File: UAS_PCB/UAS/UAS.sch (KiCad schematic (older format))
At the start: 0 parts

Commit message: uas pcb files updated to latest version in ranis hellscape
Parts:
- added J1, J2, J3, J4: SM02B-PASS-TBT, UAS:JST_SM02B-PASS-TBT(LF)(SN), symbol UAS-rescue:SM02B-PASS-TBT-UAS-cache
- added U1, U8: JST-7-Pin, UAS:JST_SM07B-PASS-TBT(LF)(SN), symbol UAS-rescue:JST-7-Pin-UAS-cache
- added U10: UAS-rescue_7.5V-2.4A-Converter-UAS-cache, UAS:Pololu_7.75V_2.4A_Step_Down_Regulator, symbol UAS-rescue:UAS-rescue_7.5V-2.4A-Converter-UAS-cache-UAS-cache
- added U11, U9: JST-3-Pin, UAS:JST_SM03B-PASS-TBT(LF)(SN), symbol UAS-rescue:JST-3-Pin-UAS-cache
- added U12, U13: Signal-Pad, UAS:Individual_Solder_Pad, symbol UAS-rescue:Signal-Pad-UAS-cache
- added U14, U15, U16, U17: UAS-rescue_Signal-Pad-UAS-cache, UAS:Individual_Solder_Pad, symbol UAS-cache:UAS-rescue_Signal-Pad-UAS-cache
- added U2: 5A-5V-Converter, UAS:Pololu_5V_5A_Step_Down_Regulator, symbol UAS-rescue:5A-5V-Converter-UAS-cache
- added U3: 500mA-5V-Converter, UAS:Pololu_5V_500mA_Step_Down_Regulator, symbol UAS-rescue:500mA-5V-Converter-UAS-cache
- added U4: 12V-StepUp-Converter, UAS:Pololu_12V_Step_Up_Voltage_Regulator_SMT, symbol UAS-rescue:12V-StepUp-Converter-UAS-cache
- added U5: TB6612FNG-Dual-Motor-Driver, UAS:Pololu_TB6612_Dual_Motor_Driver_Carrier_SMT, symbol UAS-rescue:TB6612FNG-Dual-Motor-Driver-UAS-cache
- added U6: 16_Pad_2x8_Set-UAS-cache, UAS:16_Pad_Set_2mm_pitch, symbol UAS-rescue:UAS-rescue_16_Pad_2x8_Set-UAS-cache-UAS-cache
- added U7: UAS-rescue_JST-4-Pin-UAS-cache, UAS:JST_XH_B4B-XH-A_1x04_P2.50mm_Vertical, symbol UAS-rescue:UAS-rescue_JST-4-Pin-UAS-cache-UAS-cache
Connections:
- net labels added: +12V, +5V, +7.5V, GND
- wire segments 0 -> 141

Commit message: UAS Schematic/Footprint Updates
Nothing for the board layout has been worked on yet, schematic is done except for stuff like diodes or whatever I haven't confirmed w/ u guys
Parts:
- removed J1, J2, J3, J4: SM02B-PASS-TBT, UAS:JST_SM02B-PASS-TBT(LF)(SN), symbol UAS-rescue:SM02B-PASS-TBT-UAS-cache
- removed U1, U8: JST-7-Pin, UAS:JST_SM07B-PASS-TBT(LF)(SN), symbol UAS-rescue:JST-7-Pin-UAS-cache
- removed U6: 16_Pad_2x8_Set-UAS-cache, UAS:16_Pad_Set_2mm_pitch, symbol UAS-rescue:UAS-rescue_16_Pad_2x8_Set-UAS-cache-UAS-cache
- added J1, J3, J6, J7: SM04B-GHS-TB(LF)(SN)-, JST_SM04B-GHS-TB(LF)(SN)-, symbol UAS:SM04B-GHS-TB(LF)(SN)-
- added J2, J8: SM07B-GHS-TB(LF)(SN), JST_SM07B-GHS-TB(LF)(SN), symbol UAS:SM07B-GHS-TB(LF)(SN)
- added J4: SM08B-GHS-TB(LF)(SN), UAS:JST_SM08B-GHS-TB(LF)(SN), symbol UAS:SM08B-GHS-TB(LF)(SN)
- added J5: SM08B-GHS-TB(LF)(SN), JST_SM08B-GHS-TB(LF)(SN), symbol UAS:SM08B-GHS-TB(LF)(SN)
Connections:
- wire segments 141 -> 179

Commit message: Updates To UAS PCB
update #based
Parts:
- added D1, D2: D, Diode_SMD:D_0603_1608Metric, symbol Device:D
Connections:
- net at U13.1 (Signal_Out), U9.3: now also D1.1 (K), D1.2 (A)
- net at U11.3, U12.1 (Signal_Out): now also D2.1 (K), D2.2 (A)
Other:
- moved on the sheet: U12, U13
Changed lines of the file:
@@
 	5550 4900 6250 4900
-Wire Wire Line
-	6250 4900 6250 6400
 Wire Wire Line
 	6250 6400 3350 6400
@@
 L UAS-rescue:Signal-Pad-UAS-cache U12
 U 1 1 60391DEE
-P 4250 5500
-F 0 "U12" H 4328 5759 50  0000 L CNN
-F 1 "Signal-Pad" H 4328 5668 50  0000 L CNN
-F 2 "UAS:Individual_Solder_Pad" H 4250 5500 50  0001 C CNN
-F 3 "" H 4250 5500 50  0001 C CNN
-	1    4250 5500
+P 4250 5300
+F 0 "U12" H 4328 5559 50  0000 L CNN
+F 1 "Signal-Pad" H 4328 5468 50  0000 L CNN
+F 2 "UAS:Individual_Solder_Pad" H 4250 5300 50  0001 C CNN
+F 3 "" H 4250 5300 50  0001 C CNN
+	1    4250 5300
 	1    0    0    -1
 $EndComp
@@
 L UAS-rescue:Signal-Pad-UAS-cache U13
 U 1 1 60392D35
-P 4450 5500
-F 0 "U13" H 4528 5759 50  0000 L CNN
-F 1 "Signal-Pad" H 4528 5668 50  0000 L CNN
-F 2 "UAS:Individual_Solder_Pad" H 4450 5500 50  0001 C CNN
-F 3 "" H 4450 5500 50  0001 C CNN
-	1    4450 5500
-	1    0    0    -1
-$EndComp
-Wire Wire Line
-	4250 5600 4250 5900
-Wire Wire Line
-	4250 5900 5600 5900
+P 4450 5300
+F 0 "U13" H 4528 5559 50  0000 L CNN
+F 1 "Signal-Pad" H 4528 5468 50  0000 L CNN
+F 2 "UAS:Individual_Solder_Pad" H 4450 5300 50  0001 C CNN
+F 3 "" H 4450 5300 50  0001 C CNN
+	1    4450 5300
+	1    0    0    -1
+$EndComp
 Wire Wire Line
 	5600 5900 5600 5550
-Wire Wire Line
-	4850 5550 4850 5700
-Wire Wire Line
-	4850 5700 4450 5700
-Wire Wire Line
-	4450 5700 4450 5600
 $Comp
 L power:GND #PWR0101
@@
 $EndComp
 Connection ~ 5350 6000
-$Comp
-L UAS-cache:UAS-rescue_Signal-Pad-UAS-cache U17
-U 1 1 603DAF7F
-P 5600 3750
-F 0 "U17" H 5512 3916 50  0000 R CNN
-F 1 "UAS-rescue_Signal-Pad-UAS-cache" H 5512 4007 50  0000 R CNN
-F 2 "UAS:Individual_Solder_Pad" H 5600 3750 50  0001 C CNN
-F 3 "" H 5600 3750 50  0001 C CNN
-	1    5600 3750
-	-1   0    0    1
-$EndComp
-$Comp
-L UAS-cache:UAS-rescue_Signal-Pad-UAS-cache U15
-U 1 1 603D9E61
-P 5300 3750
-F 0 "U15" H 5212 3916 50  0000 R CNN
-F 1 "UAS-rescue_Signal-Pad-UAS-cache" H 5212 4007 50  0000 R CNN
-F 2 "UAS:Individual_Solder_Pad" H 5300 3750 50  0001 C CNN
-F 3 "" H 5300 3750 50  0001 C CNN
-	1    5300 3750
-	-1   0    0    1
-$EndComp
-$Comp
-L UAS-cache:UAS-rescue_Signal-Pad-UAS-cache U16
-U 1 1 603D9324
-P 5600 3350
-F 0 "U16" H 5678 3609 50  0000 L CNN
-F 1 "UAS-rescue_Signal-Pad-UAS-cache" H 5678 3518 50  0000 L CNN
-F 2 "UAS:Individual_Solder_Pad" H 5600 3350 50  0001 C CNN
-F 3 "" H 5600 3350 50  0001 C CNN
-	1    5600 3350
-	1    0    0    -1
-$EndComp
-$Comp
-L UAS-cache:UAS-rescue_Signal-Pad-UAS-cache U14
-U 1 1 603D8772
-P 5300 3350
-F 0 "U14" H 5378 3609 50  0000 L CNN
-F 1 "UAS-rescue_Signal-Pad-UAS-cache" H 5378 3518 50  0000 L CNN
-F 2 "UAS:Individual_Solder_Pad" H 5300 3350 50  0001 C CNN
-F 3 "" H 5300 3350 50  0001 C CNN
-	1    5300 3350
-	1    0    0    -1
-$EndComp
-Wire Wire Line
-	5300 3450 5300 3650
-Wire Wire Line
-	5600 3450 5600 3650
 $Comp
 L UAS:SM07B-GHS-TB(LF)(SN) J2
@@
 	0    -1   -1   0
 $EndComp
+Wire Wire Line
+	6250 4900 6250 6400
+$Comp
+L Device:D D2
+U 1 1 606E7312
+P 4650 6050
+F 0 "D2" H 4650 5834 50  0000 C CNN
+F 1 "D" H 4650 5925 50  0000 C CNN
+F 2 "Diode_SMD:D_0603_1608Metric" H 4650 6050 50  0001 C CNN
+F 3 "~" H 4650 6050 50  0001 C CNN
+	1    4650 6050
+	-1   0    0    1
+$EndComp
+Wire Wire Line
+	4850 5550 4850 5600
+$Comp
+L Device:D D1
+U 1 1 6073A3FE
+P 4650 5700
+F 0 "D1" H 4650 5484 50  0000 C CNN
+F 1 "D" H 4650 5575 50  0000 C CNN
+F 2 "Diode_SMD:D_0603_1608Metric" H 4650 5700 50  0001 C CNN
+F 3 "~" H 4650 5700 50  0001 C CNN
+	1    4650 5700
+	-1   0    0    1
+$EndComp
+Wire Wire Line
+	4450 5600 4450 5400
+Wire Wire Line
+	4250 5400 4250 5900
+Wire Wire Line
+	5600 3450 5600 3650
+Wire Wire Line
+	5300 3450 5300 3650
+$Comp
+L UAS-cache:UAS-rescue_Signal-Pad-UAS-cache U14
+U 1 1 603D8772
+P 5300 3350
+F 0 "U14" H 5378 3609 50  0000 L CNN
+F 1 "UAS-rescue_Signal-Pad-UAS-cache" H 5378 3518 50  0000 L CNN
+F 2 "UAS:Individual_Solder_Pad" H 5300 3350 50  0001 C CNN
+F 3 "" H 5300 3350 50  0001 C CNN
+	1    5300 3350
+	1    0    0    -1
+$EndComp
+$Comp
+L UAS-cache:UAS-rescue_Signal-Pad-UAS-cache U16
+U 1 1 603D9324
+P 5600 3350
+F 0 "U16" H 5678 3609 50  0000 L CNN
+F 1 "UAS-rescue_Signal-Pad-UAS-cache" H 5678 3518 50  0000 L CNN
+F 2 "UAS:Individual_Solder_Pad" H 5600 3350 50  0001 C CNN
+F 3 "" H 5600 3350 50  0001 C CNN
+	1    5600 3350
+	1    0    0    -1
+$EndComp
+$Comp
+L UAS-cache:UAS-rescue_Signal-Pad-UAS-cache U15
+U 1 1 603D9E61
+P 5300 3750
+F 0 "U15" H 5212 3916 50  0000 R CNN
+F 1 "UAS-rescue_Signal-Pad-UAS-cache" H 5212 4007 50  0000 R CNN
+F 2 "UAS:Individual_Solder_Pad" H 5300 3750 50  0001 C CNN
+F 3 "" H 5300 3750 50  0001 C CNN
+	1    5300 3750
+	-1   0    0    1
+$EndComp
+$Comp
+L UAS-cache:UAS-rescue_Signal-Pad-UAS-cache U17
+U 1 1 603DAF7F
+P 5600 3750
+F 0 "U17" H 5512 3916 50  0000 R CNN
+F 1 "UAS-rescue_Signal-Pad-UAS-cache" H 5512 4007 50  0000 R CNN
+F 2 "UAS:Individual_Solder_Pad" H 5600 3750 50  0001 C CNN
+F 3 "" H 5600 3750 50  0001 C CNN
+	1    5600 3750
+	-1   0    0    1
+$EndComp
+Wire Wire Line
+	4250 5900 4450 5900
+Wire Wire Line
+	4800 6050 4850 6050
+Wire Wire Line
+	4850 6050 4850 5900
+Connection ~ 4850 5900
+Wire Wire Line
+	4850 5900 5600 5900
+Wire Wire Line
+	4500 6050 4450 6050
+Wire Wire Line
+	4450 6050 4450 5900
+Connection ~ 4450 5900
+Wire Wire Line
+	4450 5900 4850 5900
+Wire Wire Line
+	4500 5700 4450 5700
+Wire Wire Line
+	4450 5700 4450 5600
+Connection ~ 4450 5600
+Wire Wire Line
+	4450 5600 4850 5600
+Wire Wire Line
+	4800 5700 4850 5700
+Wire Wire Line
+	4850 5700 4850 5600
+Connection ~ 4850 5600
 $EndSCHEMATC

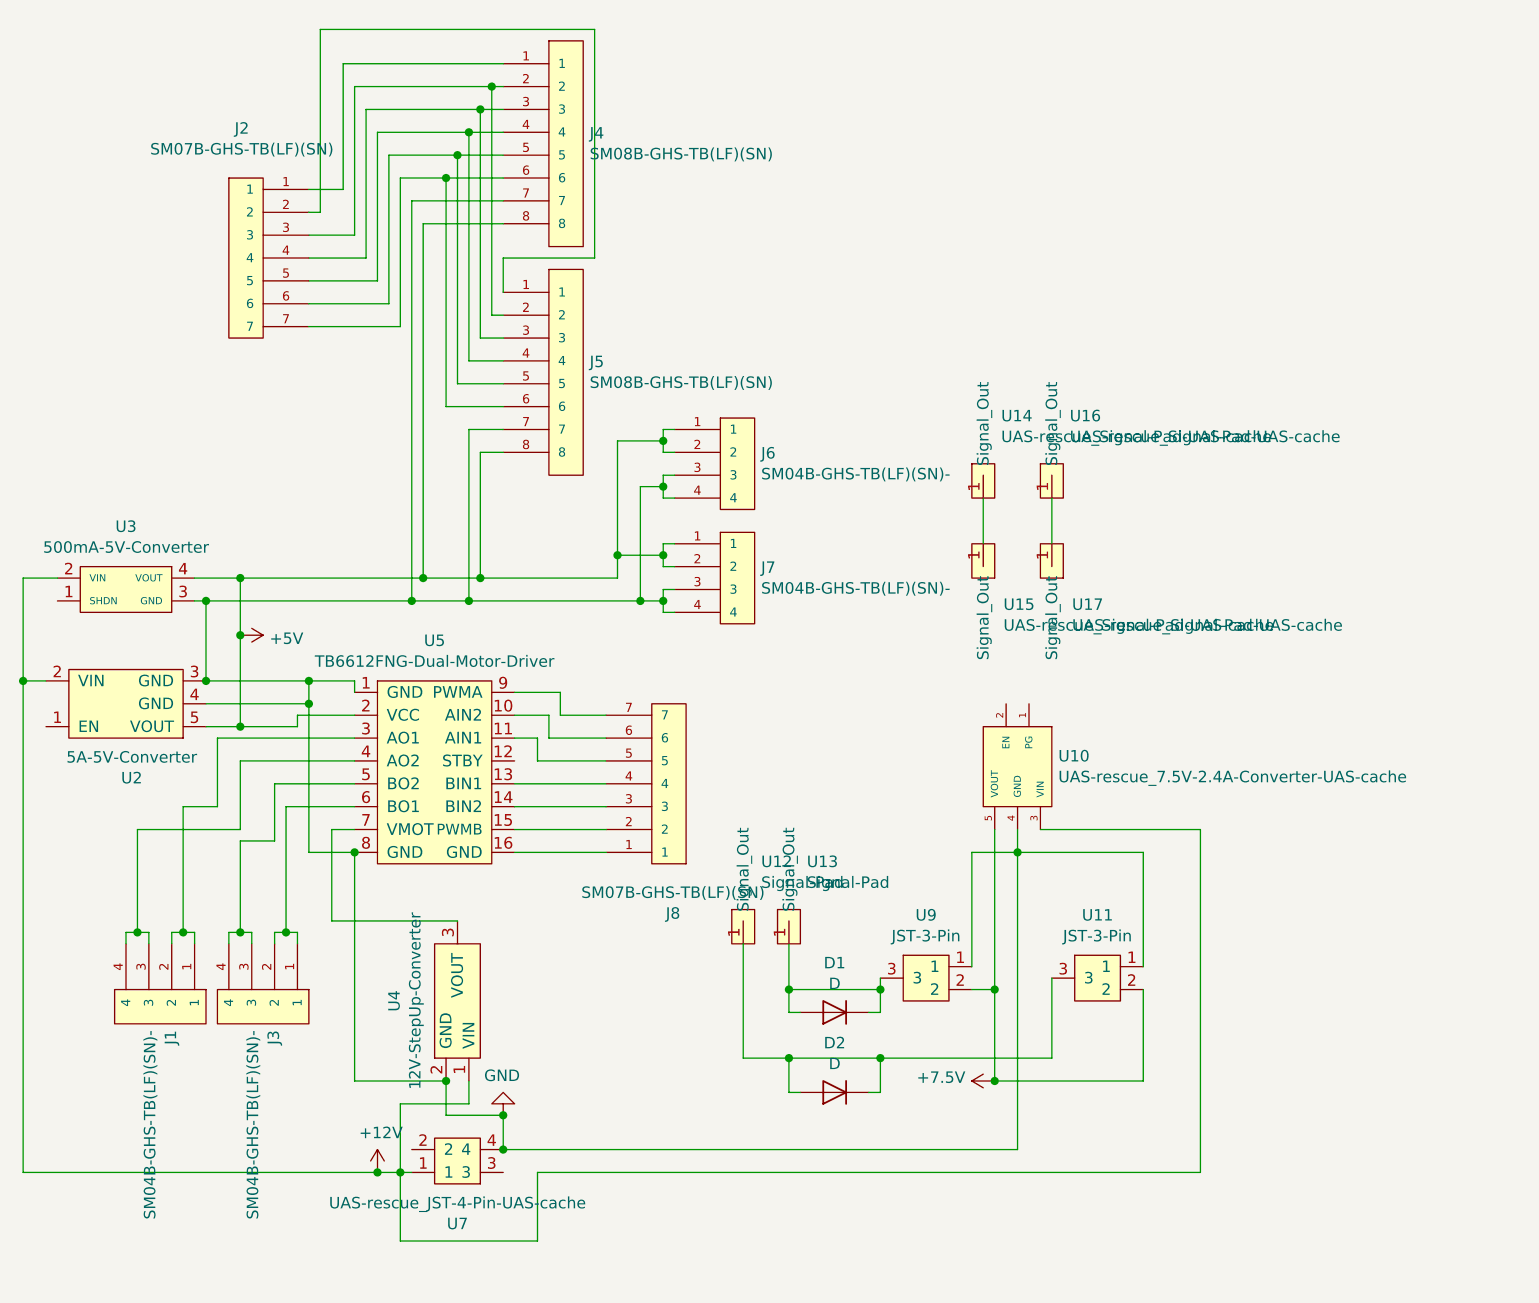
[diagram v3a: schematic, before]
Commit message: Removing Diodes
Just removing the diodes from schematic
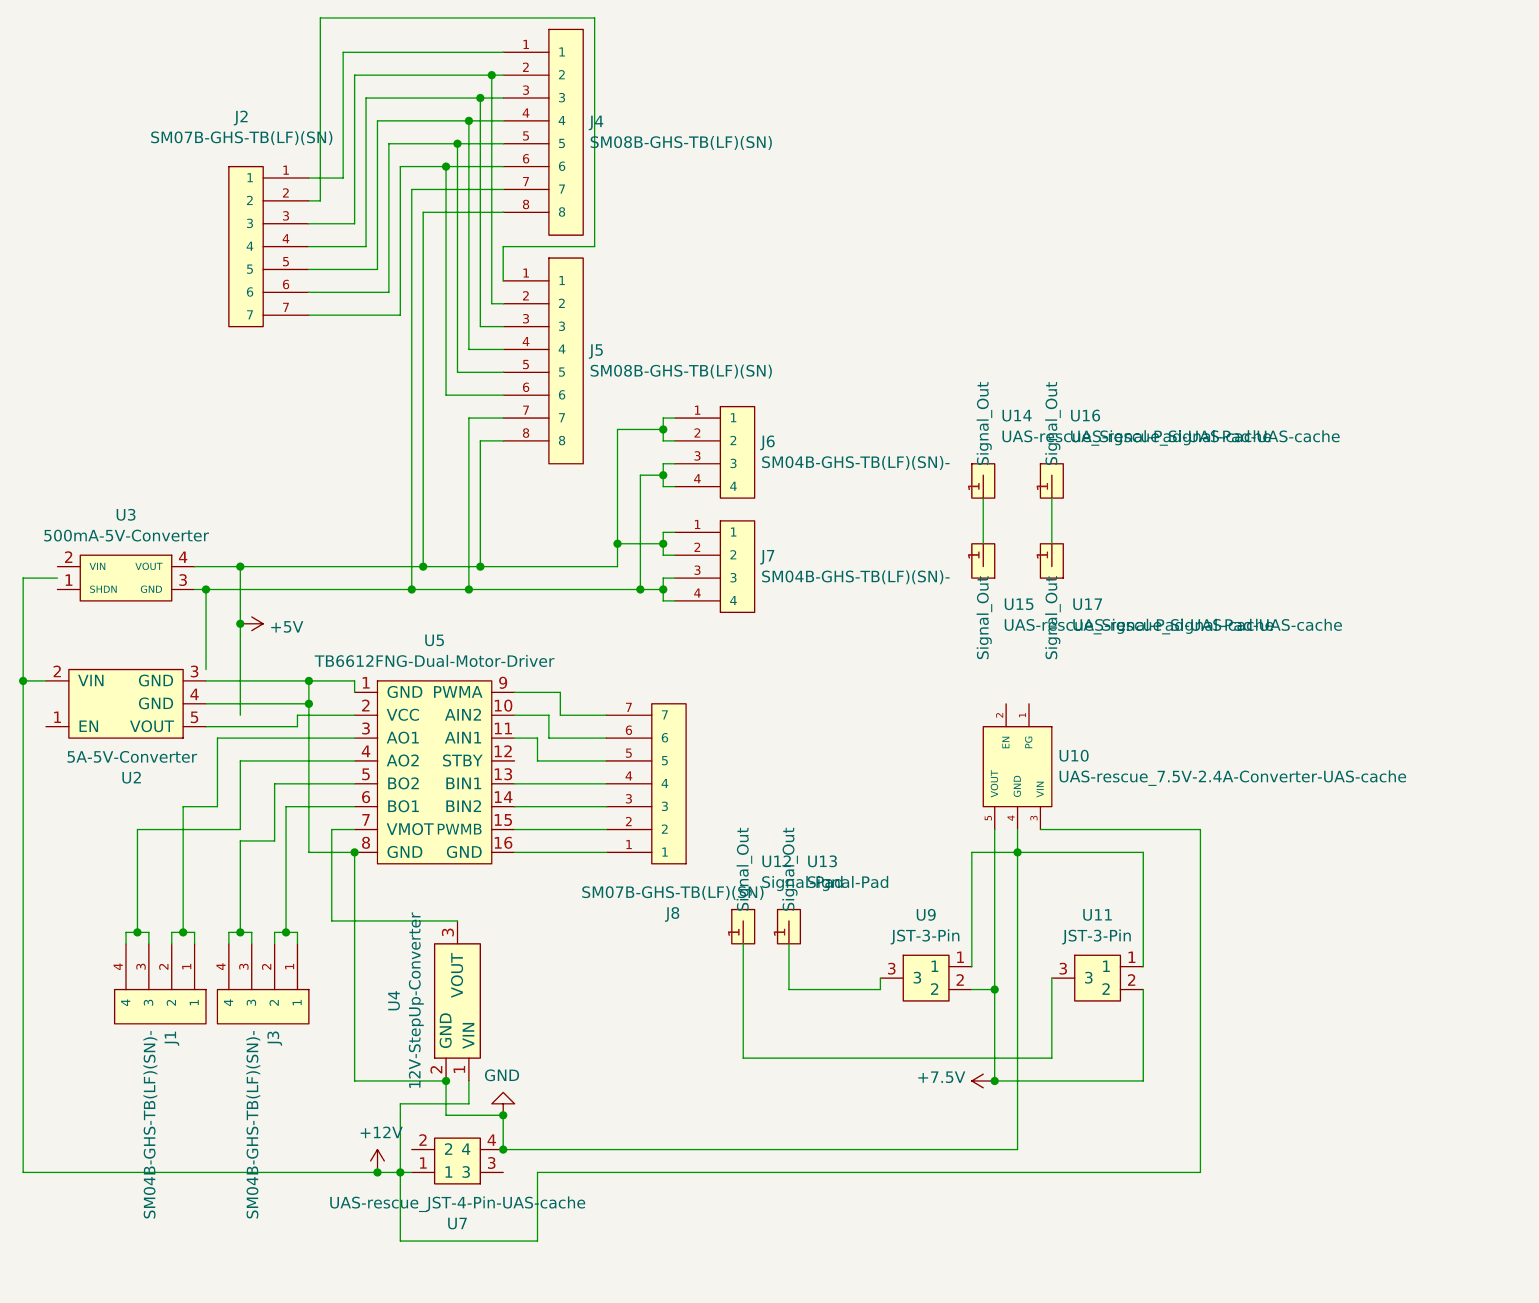
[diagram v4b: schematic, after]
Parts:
- removed D1, D2: D, Diode_SMD:D_0603_1608Metric, symbol Device:D
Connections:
- net +12V: no longer U3.2 (VIN)
- net +5V: no longer U2.5 (VOUT), U5.2 (VCC)
- net GND: no longer J4.7, J5.7, J6.3, J6.4, J7.3, J7.4, U3.3 (GND)
- new net: U2.5 (VOUT), U5.2 (VCC)
- new net: J4.7, J5.7, J6.3, J6.4, J7.3, J7.4, U3.3 (GND)
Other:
- moved on the sheet: J2, J4, J5, J6, J7, U3

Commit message: JST 3-Pin cleanup
I cleaned it (?)
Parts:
- removed U14, U15, U16, U17: UAS-rescue_Signal-Pad-UAS-cache, UAS:Individual_Solder_Pad, symbol UAS-cache:UAS-rescue_Signal-Pad-UAS-cache
- U11, U9: symbol UAS-rescue:JST-3-Pin-UAS-cache -> UAS:JST-3-pin-Revised-Symbol
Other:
- moved on the sheet: U11, U9
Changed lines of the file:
@@
-$EndComp
-$Comp
-L UAS-rescue:JST-3-Pin-UAS-cache U9
-U 1 1 6035FF82
-P 5050 5350
-F 0 "U9" H 5050 5425 50  0000 C CNN
-F 1 "JST-3-Pin" H 5050 5334 50  0000 C CNN
-F 2 "UAS:JST_SM03B-PASS-TBT(LF)(SN)" H 5050 5450 50  0001 C CNN
-F 3 "" H 5050 5450 50  0001 C CNN
-	1    5050 5350
-	1    0    0    -1
 $EndComp
 $Comp
@@
 	1    0    0    -1
 $EndComp
-$Comp
-L UAS-rescue:UAS-rescue_7.5V-2.4A-Converter-UAS-cache-UAS-cache U10
-U 1 1 6037F8BA
-P 5650 4650
-F 0 "U10" V 5579 4628 50  0000 L CNN
-F 1 "UAS-rescue_7.5V-2.4A-Converter-UAS-cache" V 5670 4628 50  0000 L CNN
-F 2 "UAS:Pololu_7.75V_2.4A_Step_Down_Regulator" H 5650 4750 50  0001 C CNN
-F 3 "" H 5650 4750 50  0001 C CNN
-	1    5650 4650
-	0    1    1    0
-$EndComp
-$Comp
-L UAS-rescue:JST-3-Pin-UAS-cache U11
-U 1 1 60369E43
-P 5800 5350
-F 0 "U11" H 5800 5425 50  0000 C CNN
-F 1 "JST-3-Pin" H 5800 5334 50  0000 C CNN
-F 2 "UAS:JST_SM03B-PASS-TBT(LF)(SN)" H 5800 5450 50  0001 C CNN
-F 3 "" H 5800 5450 50  0001 C CNN
-	1    5800 5350
-	1    0    0    -1
-$EndComp
 Wire Wire Line
 	1250 3800 1100 3800
@@
 Connection ~ 2550 5000
 Wire Wire Line
-	5250 5500 5250 5000
-Wire Wire Line
-	5250 5000 5450 5000
-Wire Wire Line
-	5450 5000 5450 4900
-Wire Wire Line
-	5250 5600 5350 5600
-Wire Wire Line
-	5350 5600 5350 4900
-Wire Wire Line
-	5550 4900 6250 4900
-Wire Wire Line
 	6250 6400 3350 6400
 Wire Wire Line
@@
 Wire Wire Line
 	3200 6300 5450 6300
-Wire Wire Line
-	5450 6300 5450 5000
 Connection ~ 3200 6300
-Connection ~ 5450 5000
-Wire Wire Line
-	5450 5000 6000 5000
-Wire Wire Line
-	6000 5000 6000 5500
-Wire Wire Line
-	5350 5600 5350 6000
-Wire Wire Line
-	5350 6000 6000 6000
-Wire Wire Line
-	6000 6000 6000 5600
-Connection ~ 5350 5600
 $Comp
 L UAS-rescue:Signal-Pad-UAS-cache U12
@@
 	1    0    0    -1
 $EndComp
-Wire Wire Line
-	5600 5900 5600 5550
 $Comp
 L power:GND #PWR0101
@@
 	0    -1   -1   0
 $EndComp
-Connection ~ 5350 6000
 $Comp
 L UAS:SM07B-GHS-TB(LF)(SN) J2
@@
 	6250 4900 6250 6400
 Wire Wire Line
-	4850 5550 4850 5600
-Wire Wire Line
-	4450 5600 4450 5400
-Wire Wire Line
 	4250 5400 4250 5900
 Wire Wire Line
-	5600 3450 5600 3650
-Wire Wire Line
-	5300 3450 5300 3650
-$Comp
-L UAS-cache:UAS-rescue_Signal-Pad-UAS-cache U14
-U 1 1 603D8772
-P 5300 3350
-F 0 "U14" H 5378 3609 50  0000 L CNN
-F 1 "UAS-rescue_Signal-Pad-UAS-cache" H 5378 3518 50  0000 L CNN
-F 2 "UAS:Individual_Solder_Pad" H 5300 3350 50  0001 C CNN
-F 3 "" H 5300 3350 50  0001 C CNN
-	1    5300 3350
-	1    0    0    -1
-$EndComp
-$Comp
-L UAS-cache:UAS-rescue_Signal-Pad-UAS-cache U16
-U 1 1 603D9324
-P 5600 3350
-F 0 "U16" H 5678 3609 50  0000 L CNN
-F 1 "UAS-rescue_Signal-Pad-UAS-cache" H 5678 3518 50  0000 L CNN
-F 2 "UAS:Individual_Solder_Pad" H 5600 3350 50  0001 C CNN
-F 3 "" H 5600 3350 50  0001 C CNN
-	1    5600 3350
-	1    0    0    -1
-$EndComp
-$Comp
-L UAS-cache:UAS-rescue_Signal-Pad-UAS-cache U15
-U 1 1 603D9E61
-P 5300 3750
-F 0 "U15" H 5212 3916 50  0000 R CNN
-F 1 "UAS-rescue_Signal-Pad-UAS-cache" H 5212 4007 50  0000 R CNN
-F 2 "UAS:Individual_Solder_Pad" H 5300 3750 50  0001 C CNN
-F 3 "" H 5300 3750 50  0001 C CNN
-	1    5300 3750
-	-1   0    0    1
-$EndComp
-$Comp
-L UAS-cache:UAS-rescue_Signal-Pad-UAS-cache U17
-U 1 1 603DAF7F
-P 5600 3750
-F 0 "U17" H 5512 3916 50  0000 R CNN
-F 1 "UAS-rescue_Signal-Pad-UAS-cache" H 5512 4007 50  0000 R CNN
-F 2 "UAS:Individual_Solder_Pad" H 5600 3750 50  0001 C CNN
-F 3 "" H 5600 3750 50  0001 C CNN
-	1    5600 3750
-	-1   0    0    1
-$EndComp
-Wire Wire Line
-	4450 5600 4850 5600
-Wire Wire Line
 	1900 4450 2300 4450
 Wire Wire Line
 	4250 5900 5600 5900
+$Comp
+L UAS:JST-3-pin-Revised-Symbol U9
+U 1 1 6035FF82
+P 5050 5350
+F 0 "U9" H 5050 5425 50  0000 C CNN
+F 1 "JST-3-Pin" H 5050 5334 50  0000 C CNN
+F 2 "UAS:JST_SM03B-PASS-TBT(LF)(SN)" H 5050 5450 50  0001 C CNN
+F 3 "" H 5050 5450 50  0001 C CNN
+	1    5050 5350
+	1    0    0    -1
+$EndComp
+Wire Wire Line
+	4700 5350 4700 5700
+Wire Wire Line
+	4700 5700 5350 5700
+Wire Wire Line
+	4700 5350 4850 5350
+Connection ~ 5350 5700
+Wire Wire Line
+	5350 5700 5350 6000
+Wire Wire Line
+	4850 5250 4750 5250
+Wire Wire Line
+	4750 5250 4750 5000
+Wire Wire Line
+	5450 5000 5450 5250
+Connection ~ 5450 5000
+Wire Wire Line
+	4750 5000 5450 5000
+Wire Wire Line
+	5450 4900 5450 5000
+$Comp
+L UAS-rescue:UAS-rescue_7.5V-2.4A-Converter-UAS-cache-UAS-cache U10
+U 1 1 6037F8BA
+P 5650 4650
+F 0 "U10" V 5579 4628 50  0000 L CNN
+F 1 "UAS-rescue_7.5V-2.4A-Converter-UAS-cache" V 5670 4628 50  0000 L CNN
+F 2 "UAS:Pololu_7.75V_2.4A_Step_Down_Regulator" H 5650 4750 50  0001 C CNN
+F 3 "" H 5650 4750 50  0001 C CNN
+	1    5650 4650
+	0    1    1    0
+$EndComp
+Connection ~ 5450 5250
+Wire Wire Line
+	5450 6300 5450 5250
+Wire Wire Line
+	5650 5250 5450 5250
+Connection ~ 5350 5350
+Wire Wire Line
+	5350 5350 5350 4900
+Wire Wire Line
+	5650 5350 5350 5350
+Wire Wire Line
+	5600 5450 5600 5900
+Wire Wire Line
+	5600 5450 5650 5450
+$Comp
+L UAS:JST-3-pin-Revised-Symbol U11
+U 1 1 60369E43
+P 5850 5350
+F 0 "U11" H 5850 5425 50  0000 C CNN
+F 1 "JST-3-Pin" H 5850 5334 50  0000 C CNN
+F 2 "UAS:JST_SM03B-PASS-TBT(LF)(SN)" H 5850 5450 50  0001 C CNN
+F 3 "" H 5850 5450 50  0001 C CNN
+	1    5850 5350
+	1    0    0    -1
+$EndComp
+Wire Wire Line
+	5550 4900 6250 4900
+Wire Wire Line
+	5350 5350 5350 5700
+Wire Wire Line
+	4850 5450 4450 5450
+Wire Wire Line
+	4450 5450 4450 5400
 $EndSCHEMATC
